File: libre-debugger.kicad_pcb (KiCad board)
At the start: 2 copper layers, 50 x 60 mm, 81 parts, among them J1 USB_C_Receptacle_USB2.0, J2 Conn_ST_STDC14, J4 Conn_01x16, Q1 2N7002, SW1 SW_SPDT, SW2 SW_Push, U1 FT2232H, U10 74LVC1G125, U11 74LVC1G125, U12 74LVC1G125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

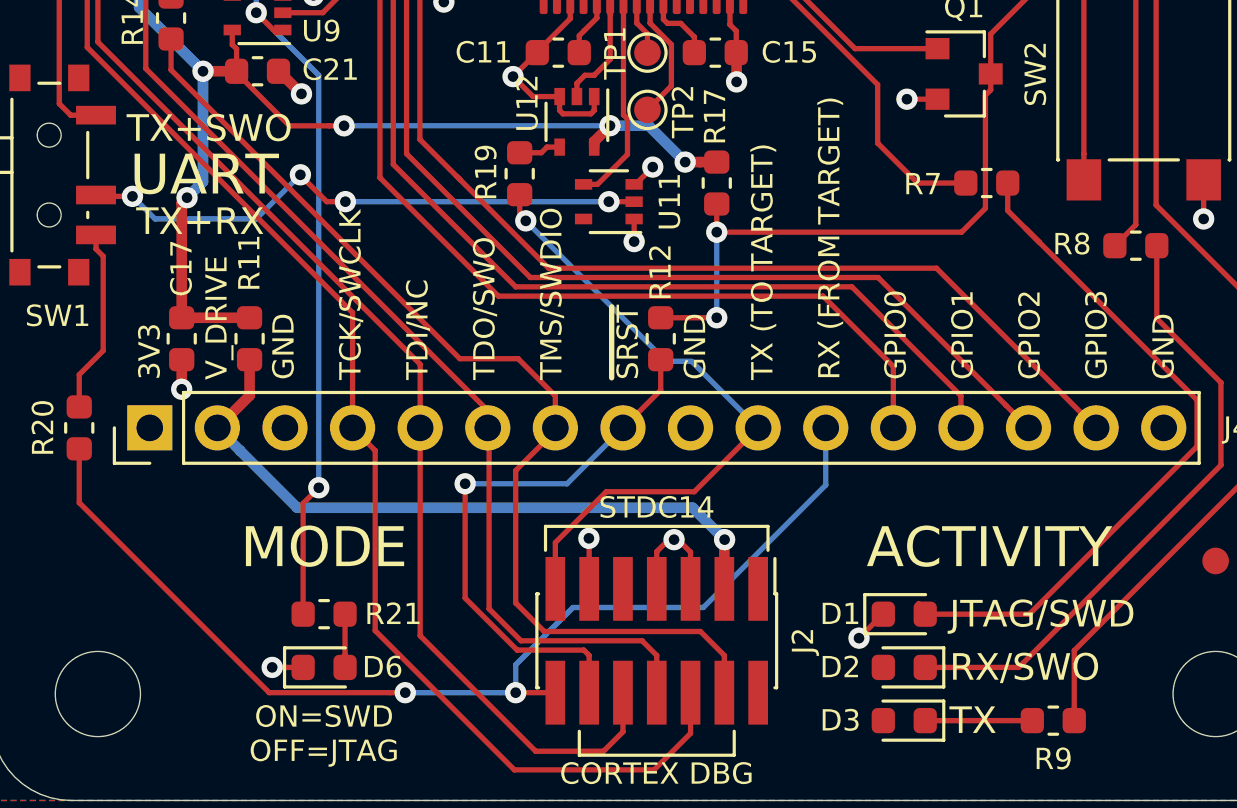
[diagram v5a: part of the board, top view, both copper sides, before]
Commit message: Make MPSSE LED active low
So that all the activity LEDs have the same orientation.
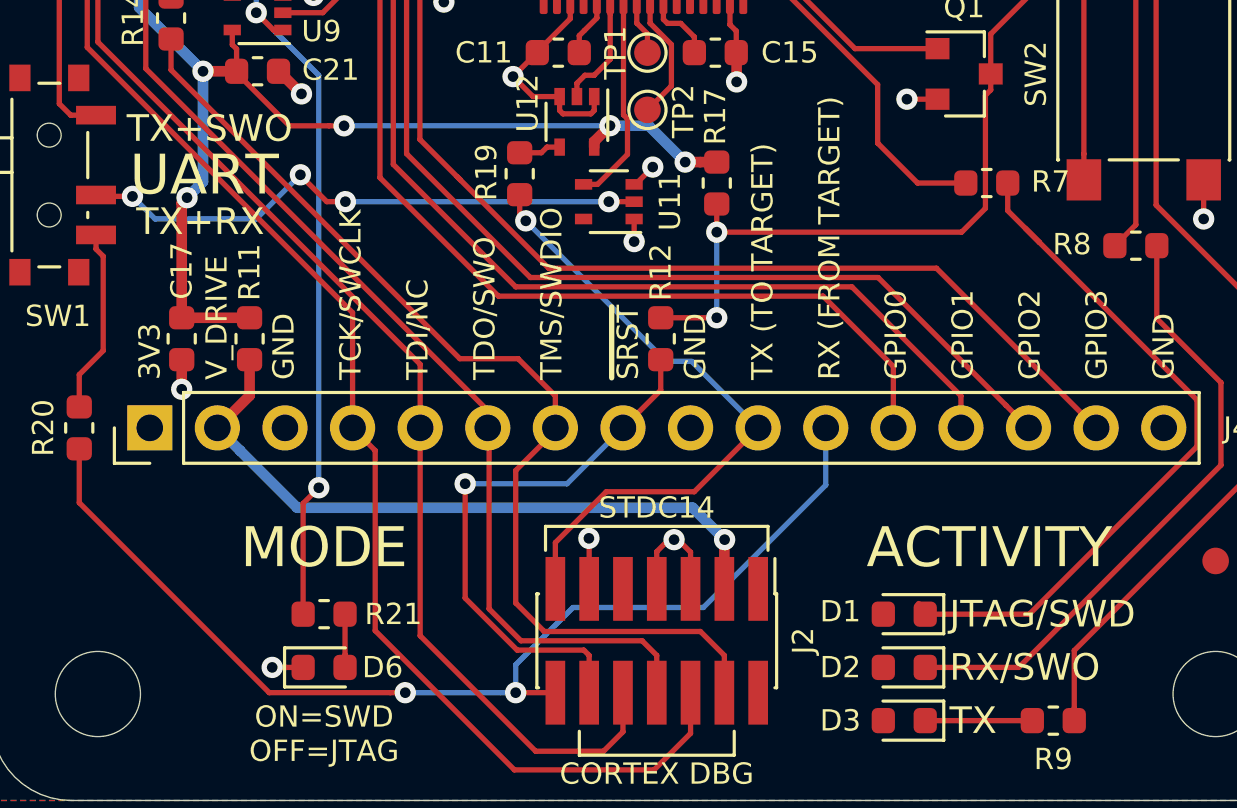
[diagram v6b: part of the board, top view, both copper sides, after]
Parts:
- turned D1 to 180 degrees
- turned R7 to 0 degrees
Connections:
- D1 pad 1: GND -> /MPSSE_LED_K
- D1 pad 2: /MPSSE_LED_A -> +3V3
- R7 pad 1: /MPSSE_LED_A -> /MPSSE_LED_N
- R7 pad 2: /MPSSE_LED -> /MPSSE_LED_K
- U1 pad 24: /MPSSE_LED -> /MPSSE_LED_N
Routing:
- net /MPSSE_LED_A: track 26.4 -> 0.00 mm
- net /MPSSE_LED_K: track 0.00 -> 26.4 mm
- net /MPSSE_LED_N: track 0.00 -> 24.5 mm
- net /MPSSE_LED: track 24.5 -> 0.00 mm
- net GND: track 118.0 -> 116.7 mm, vias 42 -> 41

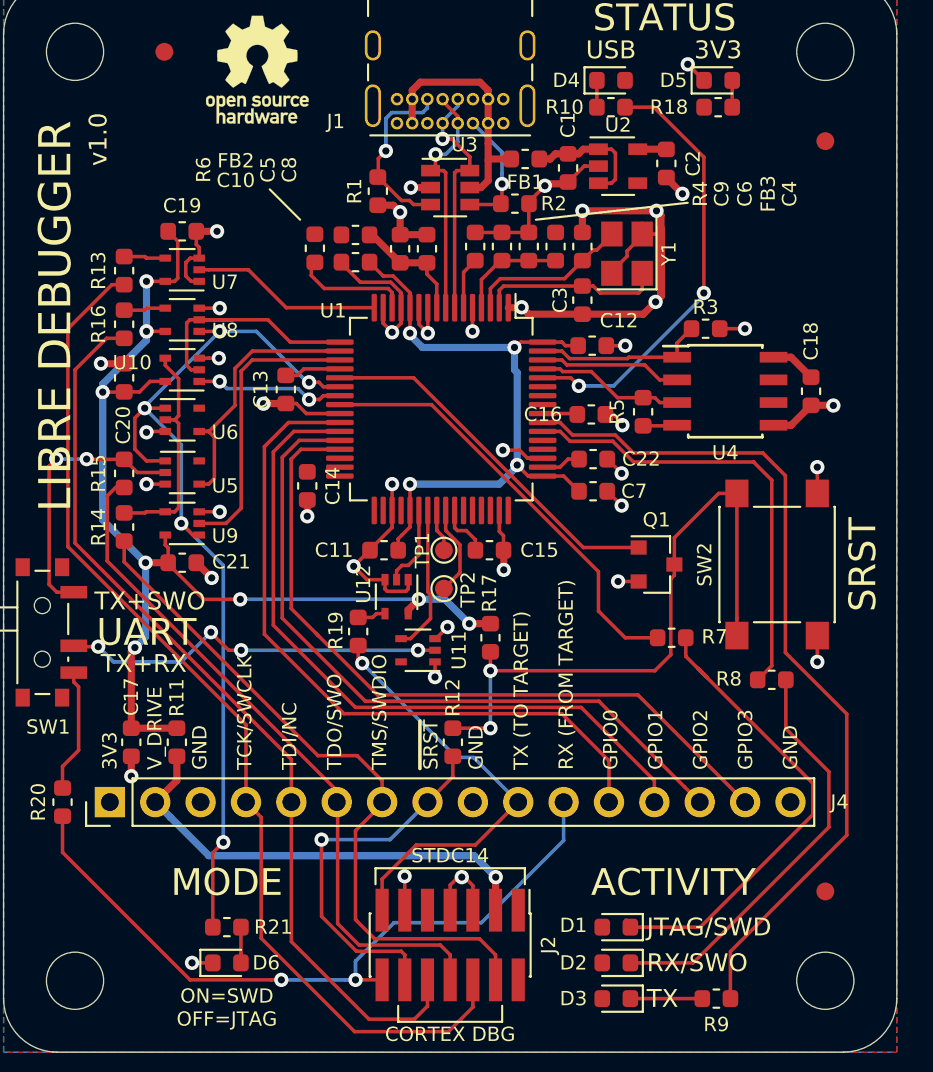
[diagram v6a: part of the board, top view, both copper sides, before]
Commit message: Add pull up on SWDIO_OE and layout clean-up
- To prevent the buffer to be active when the FTDI pin is High-Z.
- Some cleanup including silkscreen and Fab
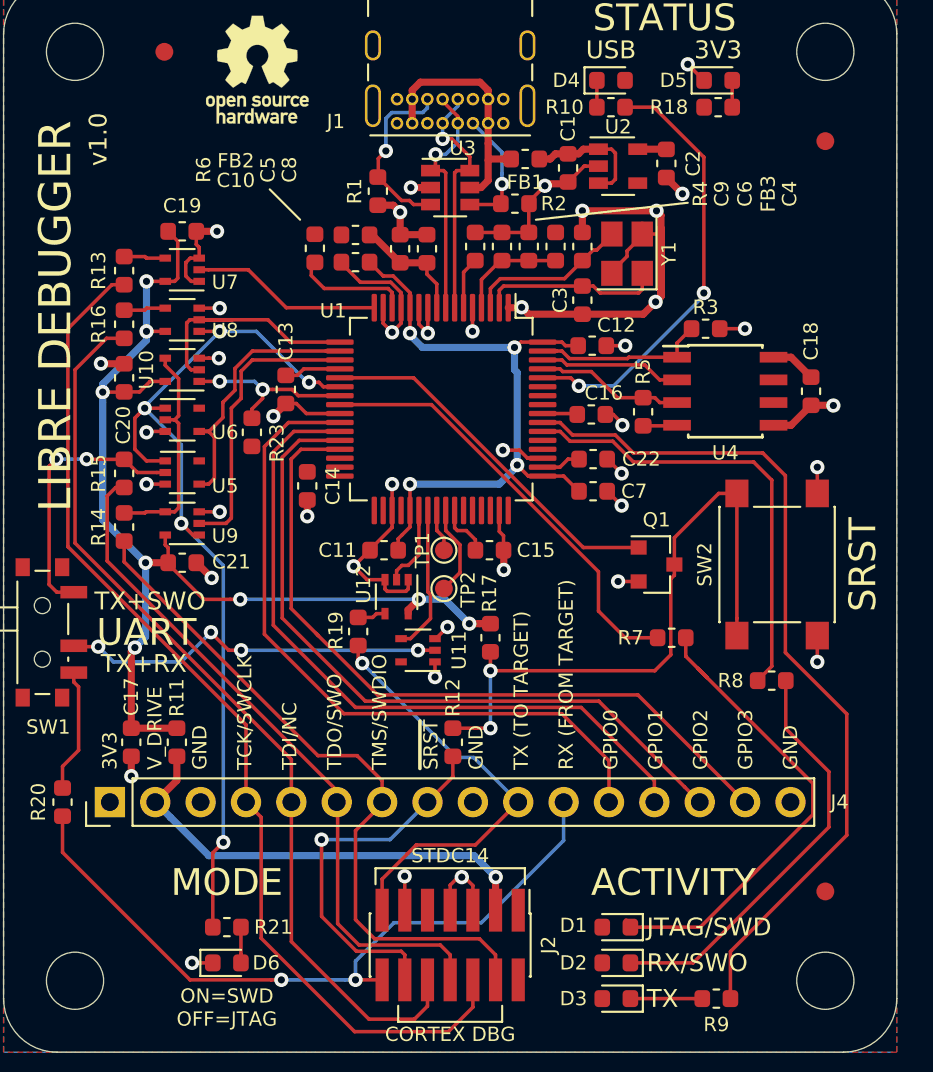
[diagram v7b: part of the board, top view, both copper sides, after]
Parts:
- added R23: 10k, Resistor_SMD:R_0603_1608Metric, F.Cu at (113.9, 75.3)
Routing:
- net /SWDIO_OE: track 8.38 -> 10.1 mm

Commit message: Go v0.1
Test this and only tag v1.0 when all OK
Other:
- board text added: "v0.1"
- board text removed: "v1.0"
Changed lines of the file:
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@@
     (effects (font (size 1 1) (thickness 0.2)) (justify mirror))
   )
-  (gr_text "v1.0" (at 105.3 58.9 90) (layer "F.SilkS")
+  (gr_text "v0.1" (at 105.3 58.9 90) (layer "F.SilkS")
     (effects (font (size 1 1) (thickness 0.2)))
   )
